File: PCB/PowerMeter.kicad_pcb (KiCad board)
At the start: 2 copper layers, 62 x 46 mm, 21 parts, among them J1 Conn_01x06_Pin, J1 Conn_02x03_Top_Bottom, J3 USB_B_Micro, SW1 SW_Push, U1 MCP1700x-330xxMB, U2 ESP32-C6-WROOM-1

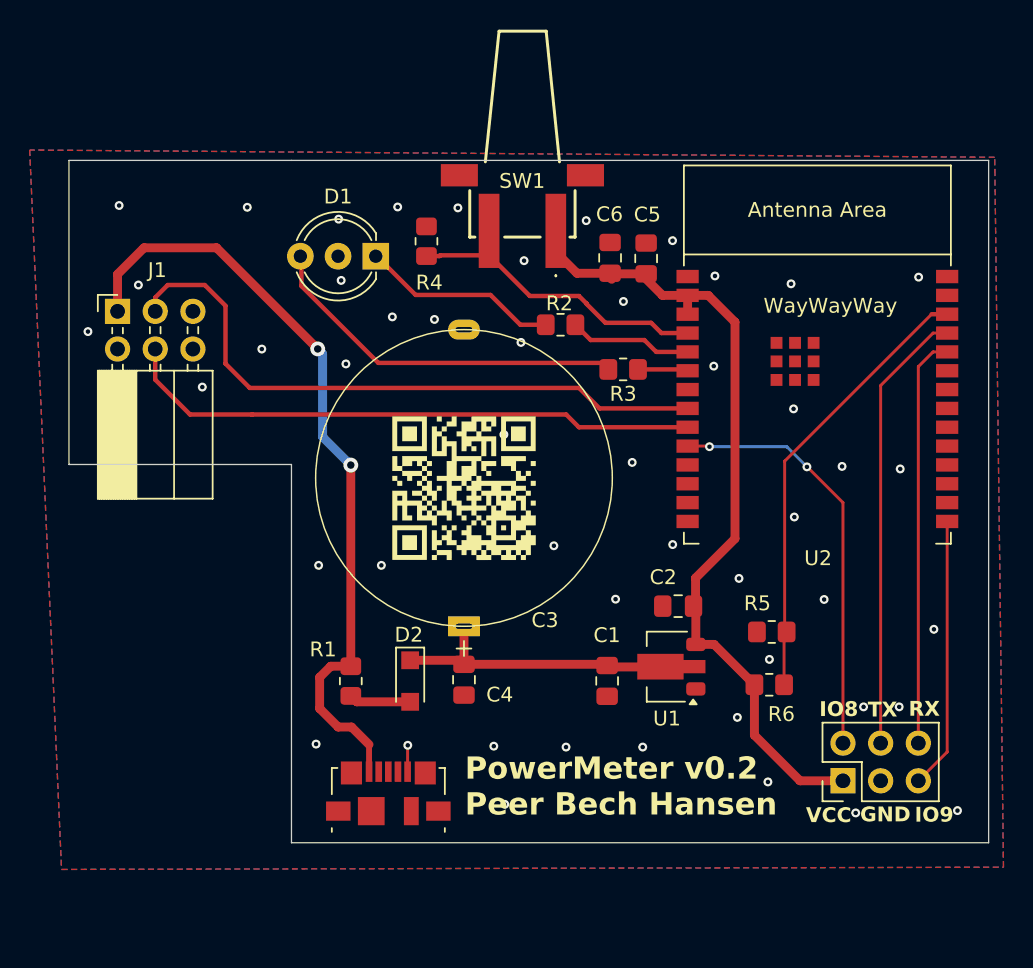
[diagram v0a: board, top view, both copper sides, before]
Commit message: Added voltage measurement for 4.1 volt
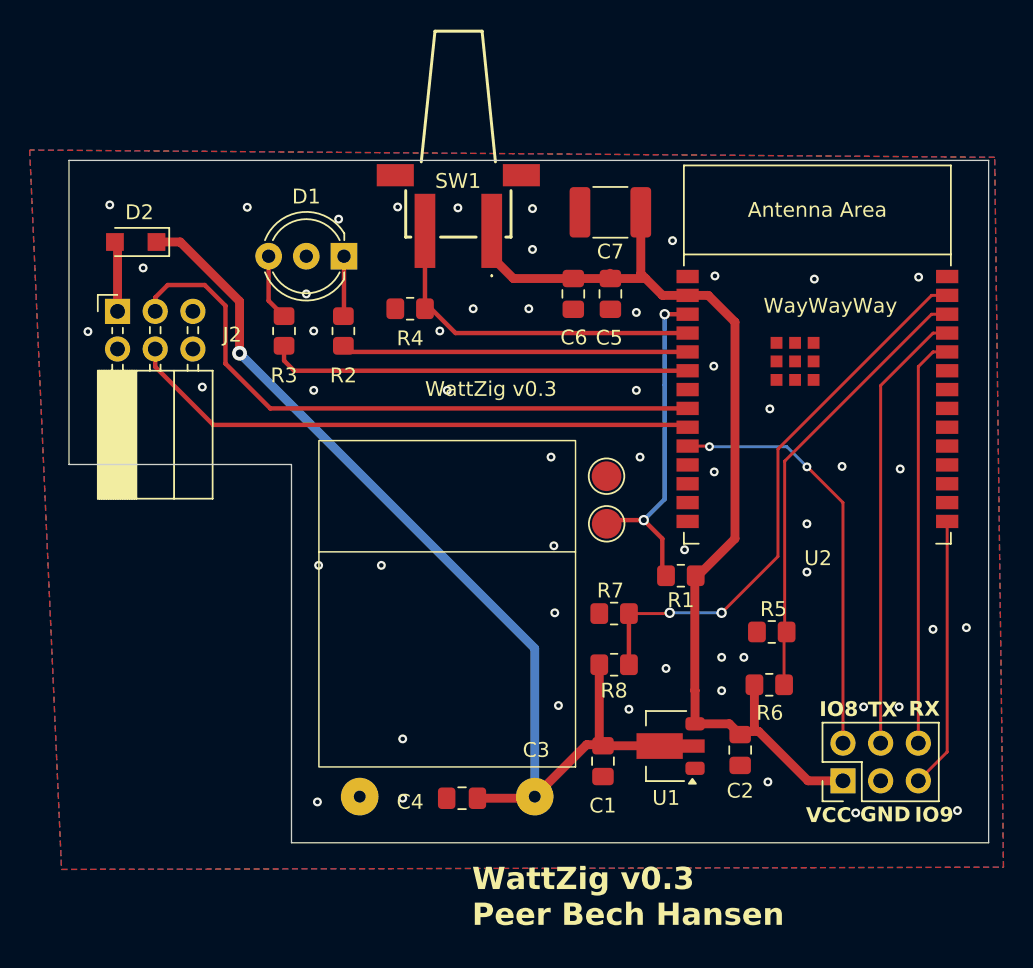
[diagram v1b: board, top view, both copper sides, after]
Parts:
- removed G***: LOGO, LOGO
- removed J3: USB_B_Micro, Connector_USB:USB_Micro-B_Molex_47346-0001
- added C7: 220µF, Capacitor_SMD:C_1812_4532Metric, F.Cu at (86.5, 53.5)
- added R7: 10K, Resistor_SMD:R_0805_2012Metric_Pad1.20x1.40mm_HandSolder, F.Cu at (86.8, 80.5)
- added R8: 10K, Resistor_SMD:R_0805_2012Metric_Pad1.20x1.40mm_HandSolder, F.Cu at (86.8, 84.0)
- added RST1: TestPoint, TestPoint:TestPoint_Pad_D2.0mm, F.Cu at (86.2, 71.3)
- added RST2: TestPoint, TestPoint:TestPoint_Pad_D2.0mm, F.Cu at (86.2, 74.5)
- C3: footprint Capacitor_THT:Peers Super -> Capacitor_THT:PHV-5R4H155-R
- R1: value 56 -> 10K
- moved D2 34.9 mm to (54.5, 55.5), turned to 180 degrees
- moved R1 23.4 mm to (91.2, 78.0), turned to 180 degrees
- moved R3 23.0 mm to (64.5, 61.5), turned to 90 degrees
- moved R2 14.6 mm to (68.5, 61.5), turned to -90 degrees
- moved C3 14.5 mm to (75.5, 90.9), turned to 180 degrees
- moved C2 10.6 mm to (95.2, 89.8), turned to -90 degrees
- moved C4 7.99 mm to (76.5, 93.0), turned to 180 degrees
- moved C1 5.42 mm to (86.0, 90.5)
- moved U1 5.35 mm to (90.3, 89.5)
- moved R4 4.68 mm to (73.0, 60.0), turned to 180 degrees
- moved SW1 4.32 mm to (76.2, 48.2)
- moved C6 3.47 mm to (84.0, 59.0), turned to -90 degrees
- moved C5 3.39 mm to (86.5, 59.0), turned to -90 degrees
- moved D1 2.14 mm to (68.5, 56.5)
- renumbered J1 to J2
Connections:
- D2 pad 2: Net-(D2-A) -> VCC
- R1 pad 1: VCC -> +3.3V
- R1 pad 2: Net-(D2-A) -> Net-(U2-EN/CHIP_PU)
- U2 pad 27: unconnected-(U2-GPIO2/ADC1_CH2-Pad27) -> Net-(U2-GPIO2/ADC1_CH2)
- U2 pad 3: +3.3V -> Net-(U2-EN/CHIP_PU)
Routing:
- net Net-(D2-K): track 22.1 -> 71.2 mm, vias 0 -> 1
- net VCC: track 52.6 -> 4.75 mm, vias 2 -> 0
- net Net-(U2-GPIO2/ADC1_CH2): track 0.00 -> 37.5 mm, vias 0 -> 2
- net Net-(U2-MTCK/GPIO6/ADC1_CH6): track 3.38 -> 28.6 mm
- net Net-(U2-EN/CHIP_PU): track 0.00 -> 23.4 mm, vias 0 -> 2
- net Net-(D1-A2): track 25.5 -> 4.47 mm
- net Net-(U2-MTDI/GPIO5/ADC1_CH5): track 8.32 -> 23.4 mm
- net +3.3V: track 57.9 -> 69.6 mm
- net Net-(D1-A1): track 13.7 -> 4.06 mm
- net Net-(D2-A): track 4.17 -> 0.00 mm
- net GND: track 1.78 -> 0.00 mm, vias 50 -> 54
- net Net-(U2-MTMS/GPIO4/ADC1_CH4): track 22.7 -> 23.6 mm
- net /DataOut: track 39.3 -> 38.8 mm
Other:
- board text added: "WattZig v0.3"
- board text added: "WattZig v0.3 Peer Bech Hansen"
- board text removed: "PowerMeter v0.2 Peer Bech Hansen"
